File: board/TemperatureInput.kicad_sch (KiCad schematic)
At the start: 18 parts, among them U4 OPA2134, U8 TL431DBZ, U9 OPA2134

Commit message: [6-5-2024] Create I/O
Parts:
- removed C3: C, Capacitor_SMD:C_01005_0402Metric_Pad0.57x0.30mm_HandSolder, symbol Device:C
- removed R10, R11, R12: 25K, Resistor_SMD:R_0805_2012Metric_Pad1.20x1.40mm_HandSolder, symbol Device:R_US
- removed unit 2 of U9
- added R14: 910, Resistor_SMD:R_0805_2012Metric_Pad1.20x1.40mm_HandSolder, symbol Device:R_US
- added R15: 100, Resistor_SMD:R_0805_2012Metric_Pad1.20x1.40mm_HandSolder, symbol Device:R_US
- C4, C5: value C -> 10n
- R8, R9: value 25K -> 1.5k
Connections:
- net GND: now also R15.2
- net PT100_OUT: now also C5.2, U9.1, R14.1
- net at U9.2 (-): now also R14.2, R15.1
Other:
- moved on the sheet: C4, C5, R8, R9, U9A

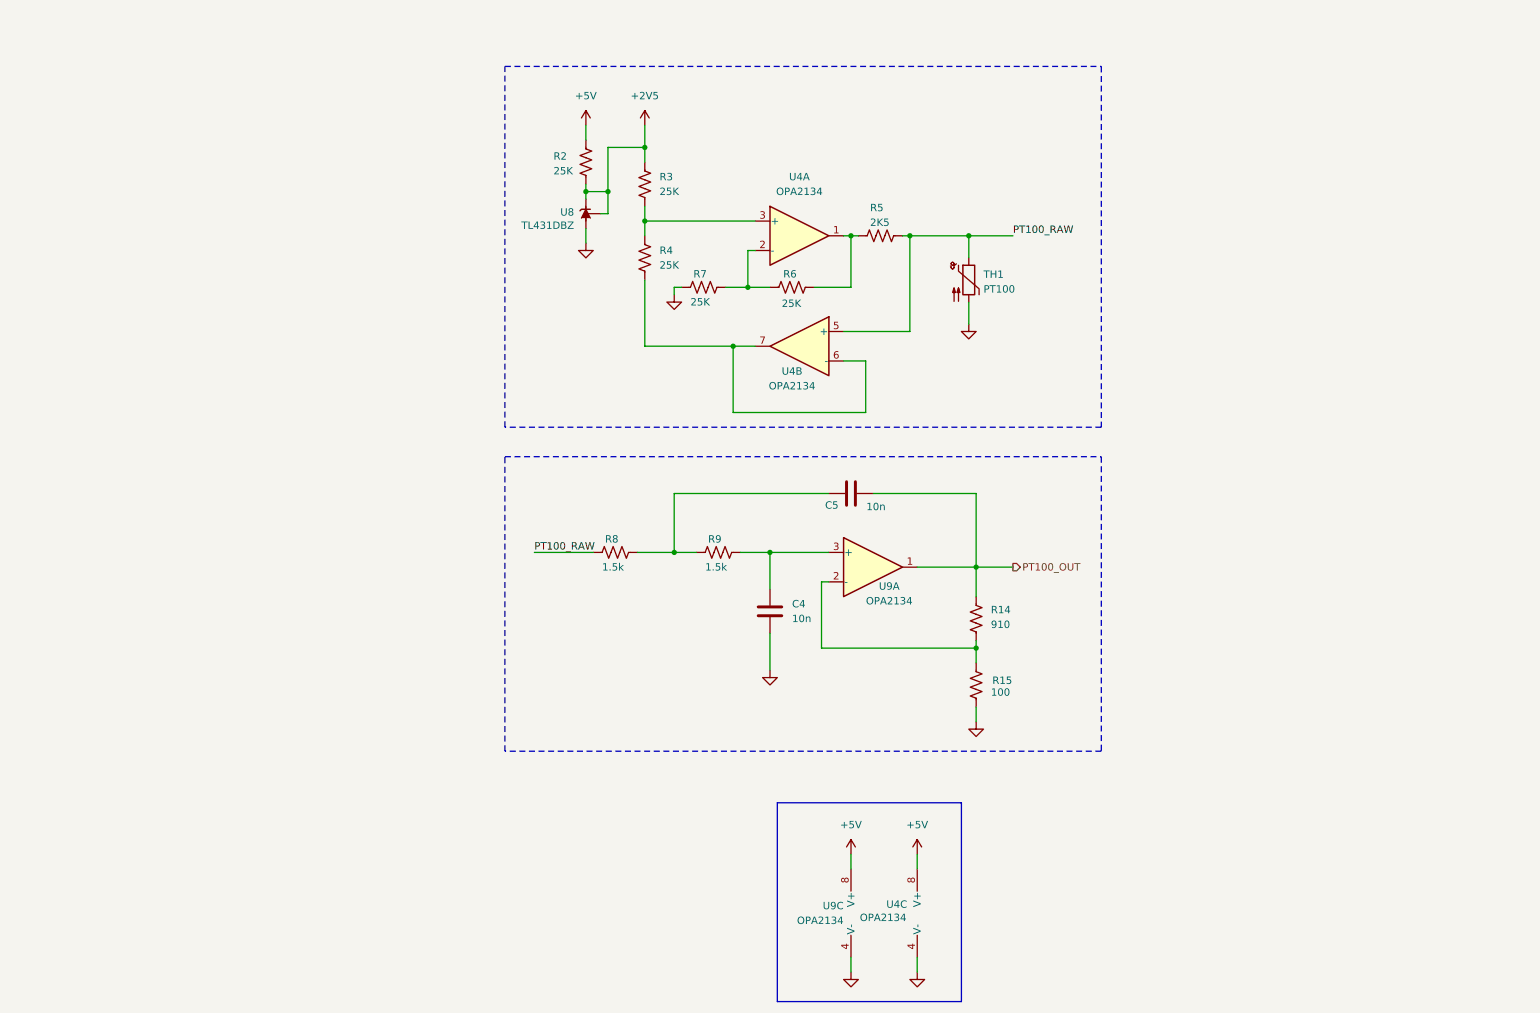
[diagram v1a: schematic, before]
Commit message: [23-5-2024] add micro sd card connector and MAX31856 Thermocouple driver
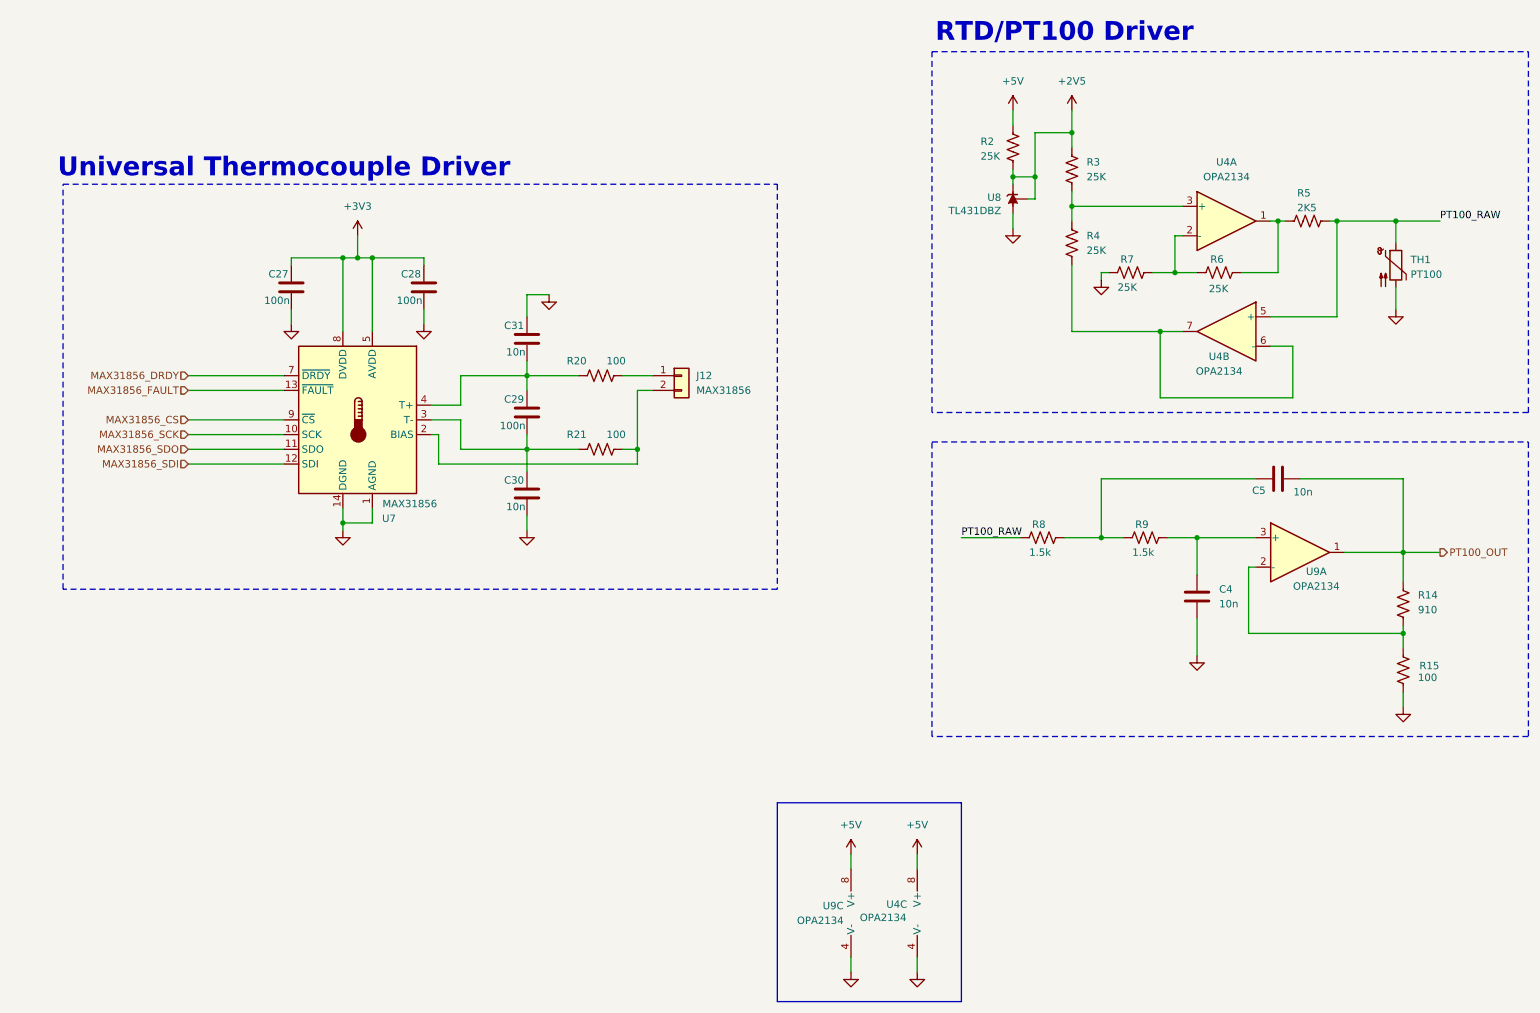
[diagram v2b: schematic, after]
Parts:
- added C27, C28, C29: 100n, Capacitor_SMD:C_01005_0402Metric_Pad0.57x0.30mm_HandSolder, symbol Device:C
- added C30, C31: 10n, Capacitor_SMD:C_01005_0402Metric_Pad0.57x0.30mm_HandSolder, symbol Device:C
- added J12: MAX31856, Connector_Wago:Wago_734-132_1x02_P3.50mm_Vertical, symbol Connector_Generic:Conn_01x02
- added R20, R21: 100, Resistor_SMD:R_0805_2012Metric_Pad1.20x1.40mm_HandSolder, symbol Device:R_US
- added U7: MAX31856, Package_SO:TSSOP-14_4.4x5mm_P0.65mm, symbol Sensor_Temperature:MAX31856
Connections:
- net GND: now also C27.2, C28.2, C30.2, C31.1, U7.1 (AGND), U7.14 (DGND)
- new net: C29.1, C31.2, R20.2, U7.4 (T+)
- new net: C29.2, C30.1, R21.2, U7.3 (T-)
- new net: J12.2 (Pin_2), R21.1, U7.2 (BIAS)
- new net: J12.1 (Pin_1), R20.1
- new net +3V3: C27.1, C28.1, U7.5 (AVDD), U7.8 (DVDD)
- new net MAX31856_CS: U7.9 (~{CS})
- new net MAX31856_DRDY: U7.7 (~{DRDY})
- new net MAX31856_FAULT: U7.13 (~{FAULT})
- new net MAX31856_SCK: U7.10 (SCK)
- new net MAX31856_SDI: U7.12 (SDI)
- new net MAX31856_SDO: U7.11 (SDO)
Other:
- note added: "RTD/PT100 Driver"
- note added: "Universal Thermocouple Driver"
- moved on the sheet: C4, C5, R14, R15, R2, R3, R4, R5, R6, R7, R8, R9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

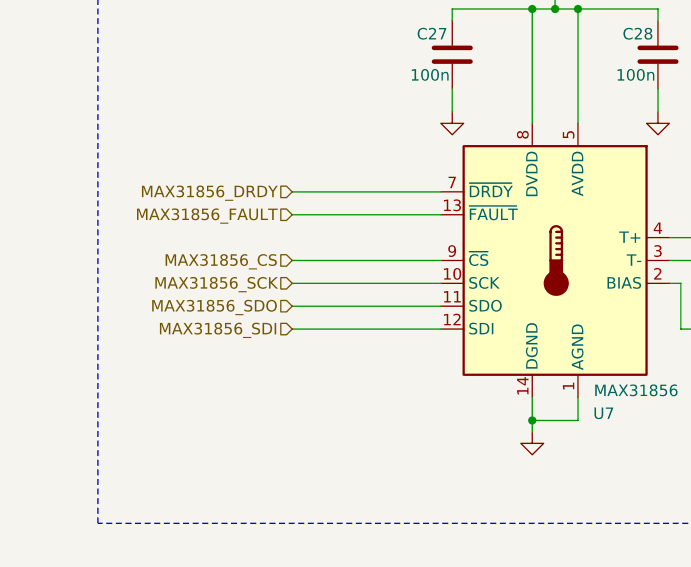
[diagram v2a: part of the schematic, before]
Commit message: [23-5-2024] add RS485 and CAN Appnote/Datasheet
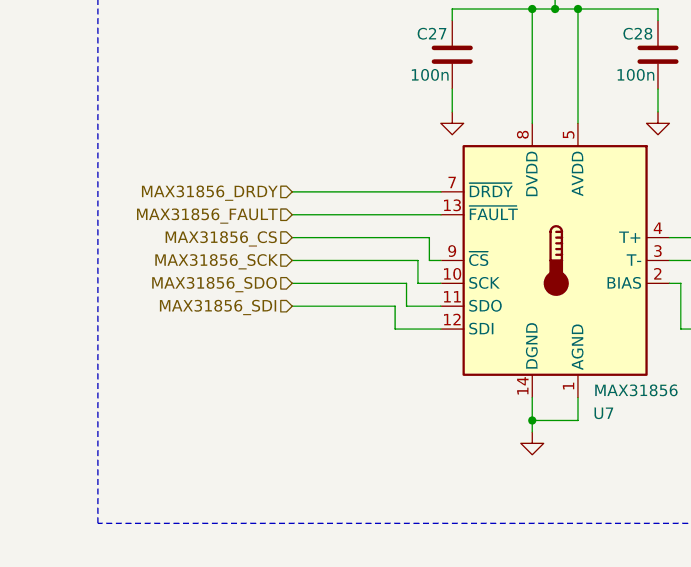
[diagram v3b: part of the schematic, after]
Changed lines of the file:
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@@
 	(wire
 		(pts
-			(xy 38.1 96.52) (xy 54.61 96.52)
+			(xy 38.1 93.98) (xy 52.07 93.98)
 		)
 		(stroke
@@
 	(wire
 		(pts
+			(xy 50.8 99.06) (xy 54.61 99.06)
+		)
+		(stroke
+			(width 0)
+			(type default)
+		)
+	)
+	(wire
+		(pts
 			(xy 184.15 55.88) (xy 182.88 55.88)
 		)
@@
 	(wire
 		(pts
+			(xy 53.34 93.98) (xy 54.61 93.98)
+		)
+		(stroke
+			(width 0)
+			(type default)
+		)
+	)
+	(wire
+		(pts
 			(xy 80.01 96.52) (xy 81.28 96.52)
 		)
@@
 	(wire
 		(pts
+			(xy 50.8 96.52) (xy 50.8 99.06)
+		)
+		(stroke
+			(width 0)
+			(type default)
+		)
+	)
+	(wire
+		(pts
 			(xy 184.15 44.45) (xy 190.5 44.45)
 		)
@@
 	(wire
 		(pts
-			(xy 38.1 99.06) (xy 54.61 99.06)
+			(xy 38.1 96.52) (xy 50.8 96.52)
 		)
 		(stroke
@@
 	(wire
 		(pts
+			(xy 49.53 101.6) (xy 54.61 101.6)
+		)
+		(stroke
+			(width 0)
+			(type default)
+		)
+	)
+	(wire
+		(pts
 			(xy 247.65 130.81) (xy 247.65 133.35)
 		)
@@
 	(wire
 		(pts
+			(xy 49.53 99.06) (xy 49.53 101.6)
+		)
+		(stroke
+			(width 0)
+			(type default)
+		)
+	)
+	(wire
+		(pts
 			(xy 180.34 40.64) (xy 180.34 43.18)
 		)
@@
 	(wire
 		(pts
-			(xy 38.1 101.6) (xy 54.61 101.6)
+			(xy 38.1 99.06) (xy 49.53 99.06)
 		)
 		(stroke
@@
 	(wire
 		(pts
+			(xy 52.07 93.98) (xy 52.07 96.52)
+		)
+		(stroke
+			(width 0)
+			(type default)
+		)
+	)
+	(wire
+		(pts
 			(xy 80.01 93.98) (xy 85.09 93.98)
 		)
@@
 	(wire
 		(pts
+			(xy 52.07 96.52) (xy 54.61 96.52)
+		)
+		(stroke
+			(width 0)
+			(type default)
+		)
+	)
+	(wire
+		(pts
 			(xy 81.28 101.6) (xy 115.57 101.6)
 		)
@@
 	(wire
 		(pts
-			(xy 38.1 93.98) (xy 54.61 93.98)
+			(xy 38.1 91.44) (xy 53.34 91.44)
 		)
 		(stroke
@@
 		(pts
 			(xy 152.4 168.91) (xy 152.4 171.45)
+		)
+		(stroke
+			(width 0)
+			(type default)
+		)
+	)
+	(wire
+		(pts
+			(xy 53.34 91.44) (xy 53.34 93.98)
 		)
 		(stroke
@@
 	(hierarchical_label "MAX31856_SDI"
 		(shape input)
-		(at 38.1 101.6 180)
+		(at 38.1 99.06 180)
 		(fields_autoplaced yes)
 		(effects
@@
 	(hierarchical_label "MAX31856_SCK"
 		(shape input)
-		(at 38.1 96.52 180)
-		(fields_autoplaced yes)
-		(effects
-			(font
-				(size 1.27 1.27)
-			)
-			(justify right)
-		)
-	)
-	(hierarchical_label "MAX31856_CS"
-		(shape input)
 		(at 38.1 93.98 180)
 		(fields_autoplaced yes)
@@
 		)
 	)
+	(hierarchical_label "MAX31856_CS"
+		(shape input)
+		(at 38.1 91.44 180)
+		(fields_autoplaced yes)
+		(effects
+			(font
+				(size 1.27 1.27)
+			)
+			(justify right)
+		)
+	)
 	(hierarchical_label "MAX31856_SDO"
 		(shape input)
-		(at 38.1 99.06 180)
+		(at 38.1 96.52 180)
 		(fields_autoplaced yes)
 		(effects
